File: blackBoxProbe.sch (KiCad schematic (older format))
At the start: 5 parts

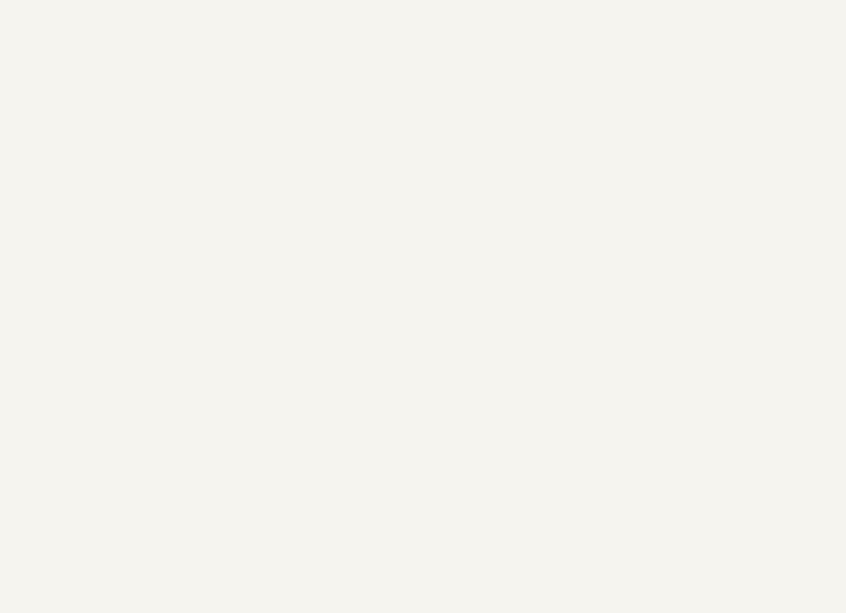
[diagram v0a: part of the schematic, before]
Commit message: * schematic layout of usb input and powersupply * PCB placing of usb input and powersupply
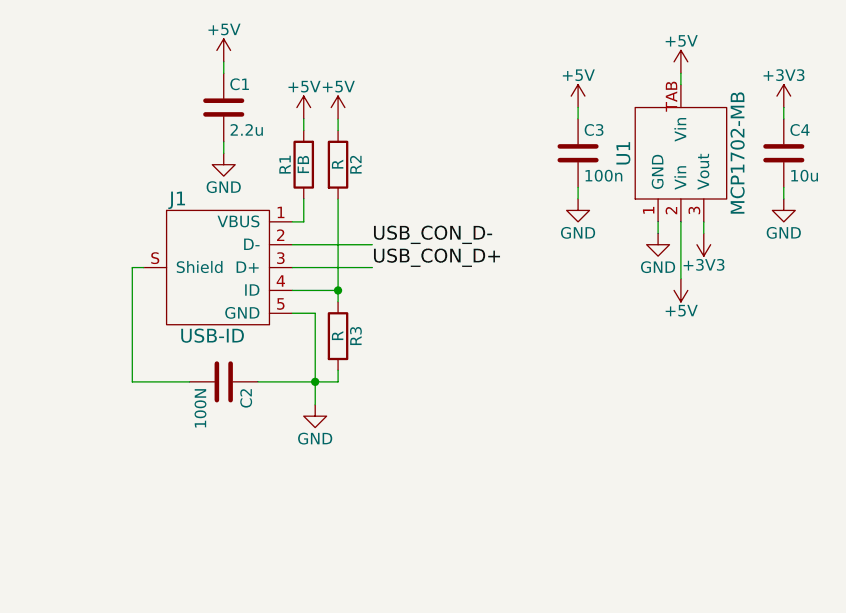
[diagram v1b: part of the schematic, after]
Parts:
- added C1: 2.2u, SquantorRcl:C_0805, symbol C
- added C2: 100N, SquantorRcl:C_0805, symbol C
- added C3: 100n, SquantorRcl:C_0603, symbol C
- added C4: 10u, SquantorRcl:C_0805, symbol C
- added J1: USB-ID, SquantorUsb:SquantorUsb-USB-UB-SMD4H, symbol USB-ID
- added R1: FB, SquantorRcl:R_0603_hand, symbol R
- added R2, R3: R, SquantorRcl:R_0603_hand, symbol R
- added U1: MCP1702-MB, SquantorMicrochip:MB-(SOT-89), symbol MCP1702-MB
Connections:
- new net: J1.1 (VBUS), R1.1
- new net: J1.4 (ID), R2.2, R3.1
- new net: C2.2, J1.S (Shield)
- new net +3V3: C4.1, U1.3 (Vout)
- new net +5V: C1.1, C3.1, R1.2, R2.1, U1.2 (Vin), U1.TAB (Vin)
- new net GND: C1.2, C2.1, C3.2, C4.2, J1.5 (GND), R3.2, U1.1 (GND)
- new net USB_CON_D+: J1.3 (D+)
- new net USB_CON_D-: J1.2 (D-)

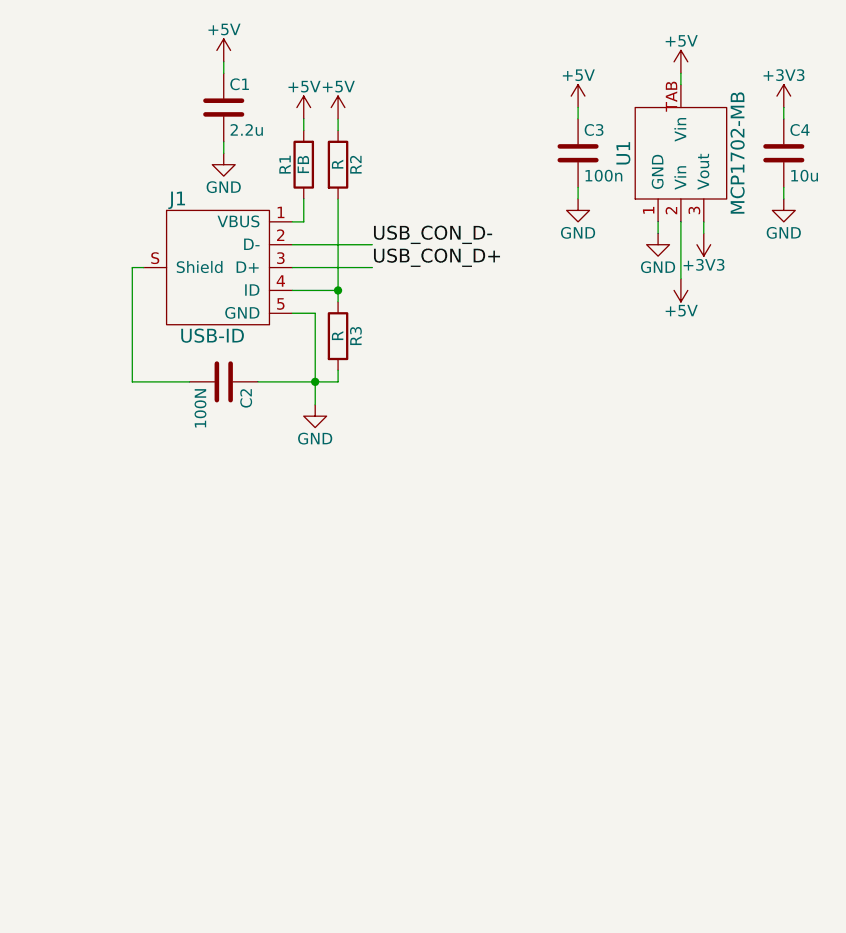
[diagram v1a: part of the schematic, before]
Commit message: * added usb protection diode
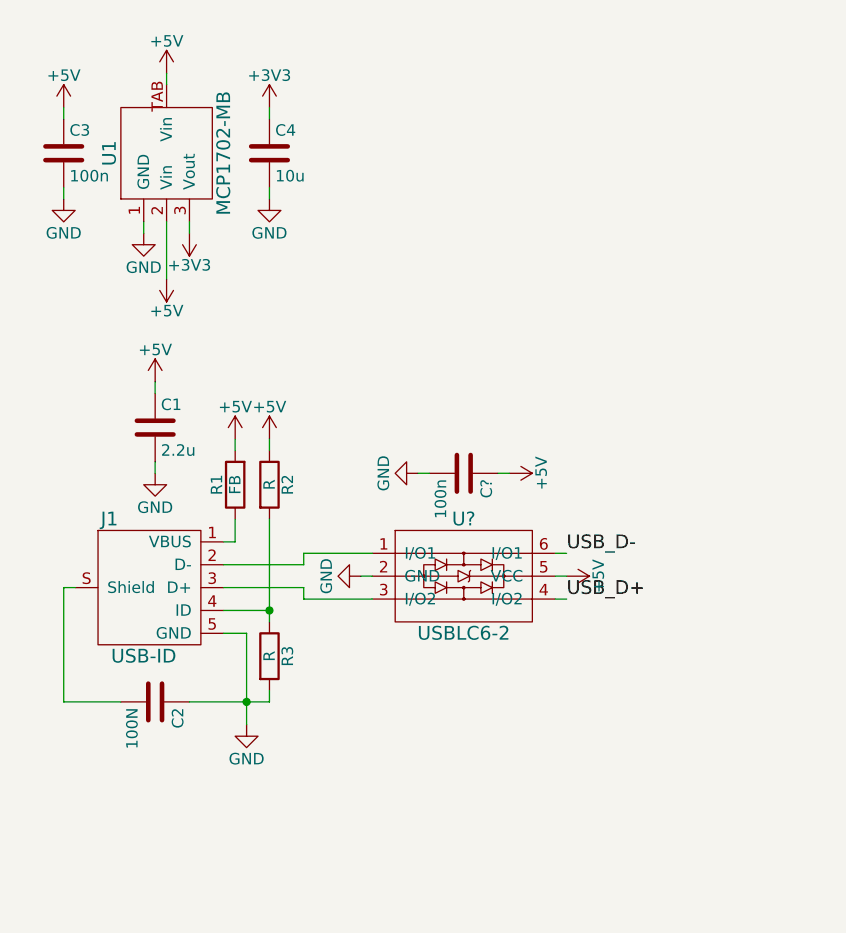
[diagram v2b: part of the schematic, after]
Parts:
- added C?: 100n, SquantorRcl:C_0603, symbol C
- added U?: USBLC6-2, symbol USBLC6-2
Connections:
- net +5V: now also C?.1, U?.5 (VCC)
- net GND: now also C?.2, U?.2 (GND)
- net USB_CON_D+: no longer names the net of J1.3 (D+)
- net USB_CON_D+: now also U?.3 (I/O2)
- net USB_CON_D-: no longer names the net of J1.2 (D-)
- net USB_CON_D-: now also U?.1 (I/O1)
- new net USB_D+: U?.4 (I/O2)
- new net USB_D-: U?.6 (I/O1)
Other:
- moved on the sheet: C1, C2, C3, C4, J1, R1, R2, R3, U1

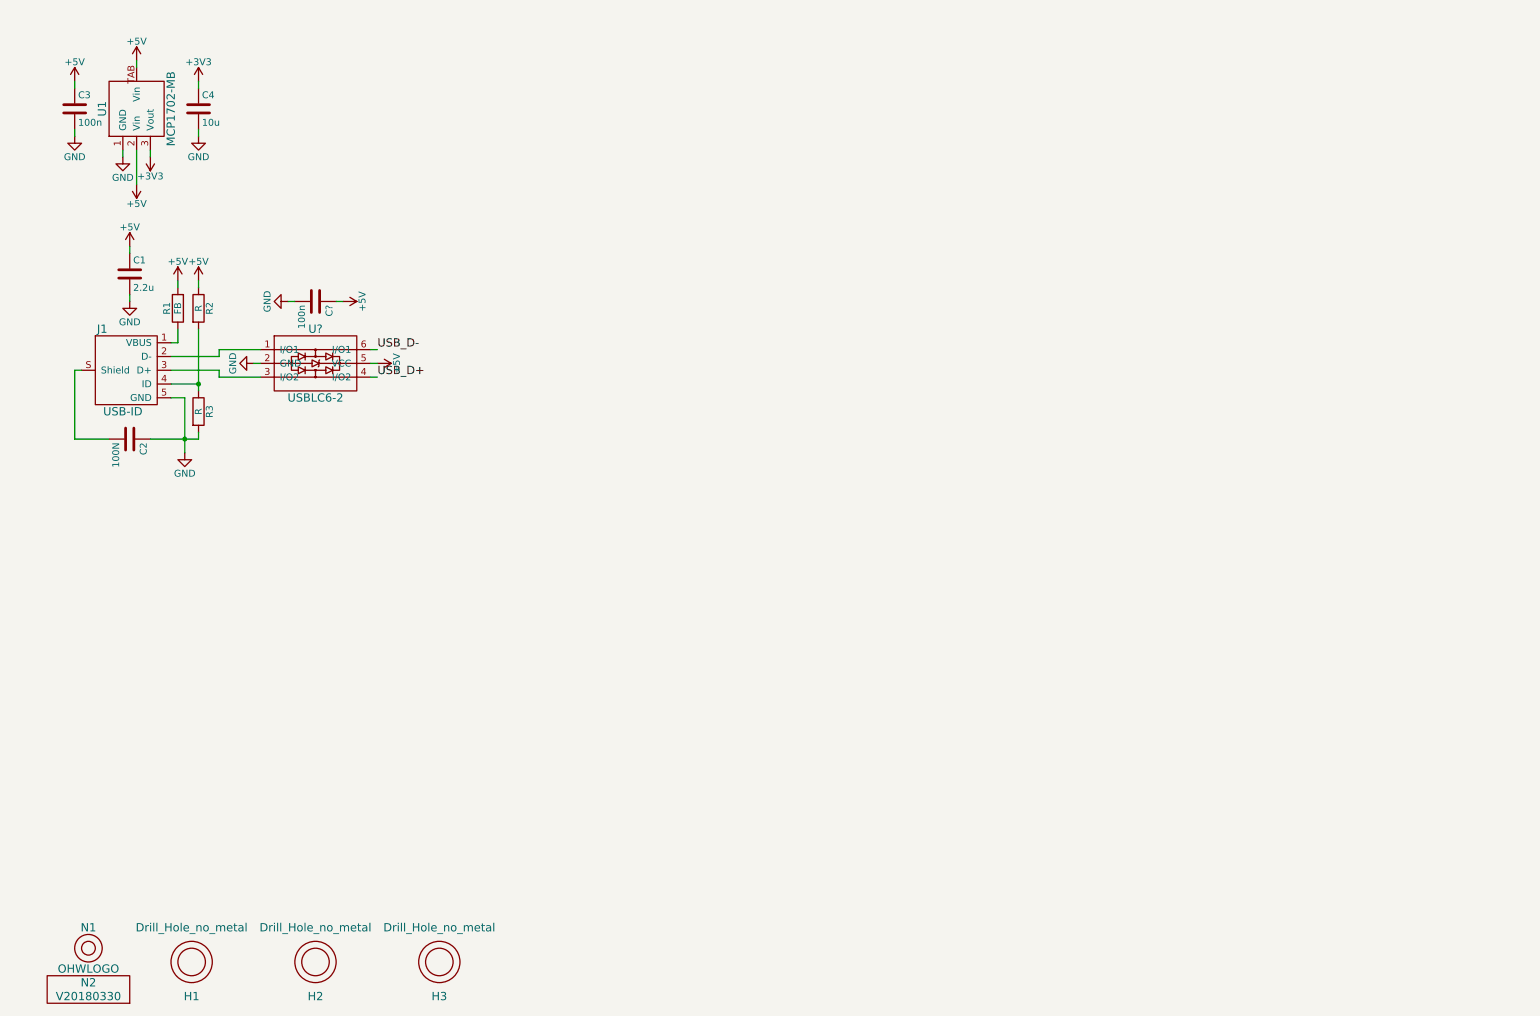
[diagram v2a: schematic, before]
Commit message: * placed controller and schematic entry of microcontroller power
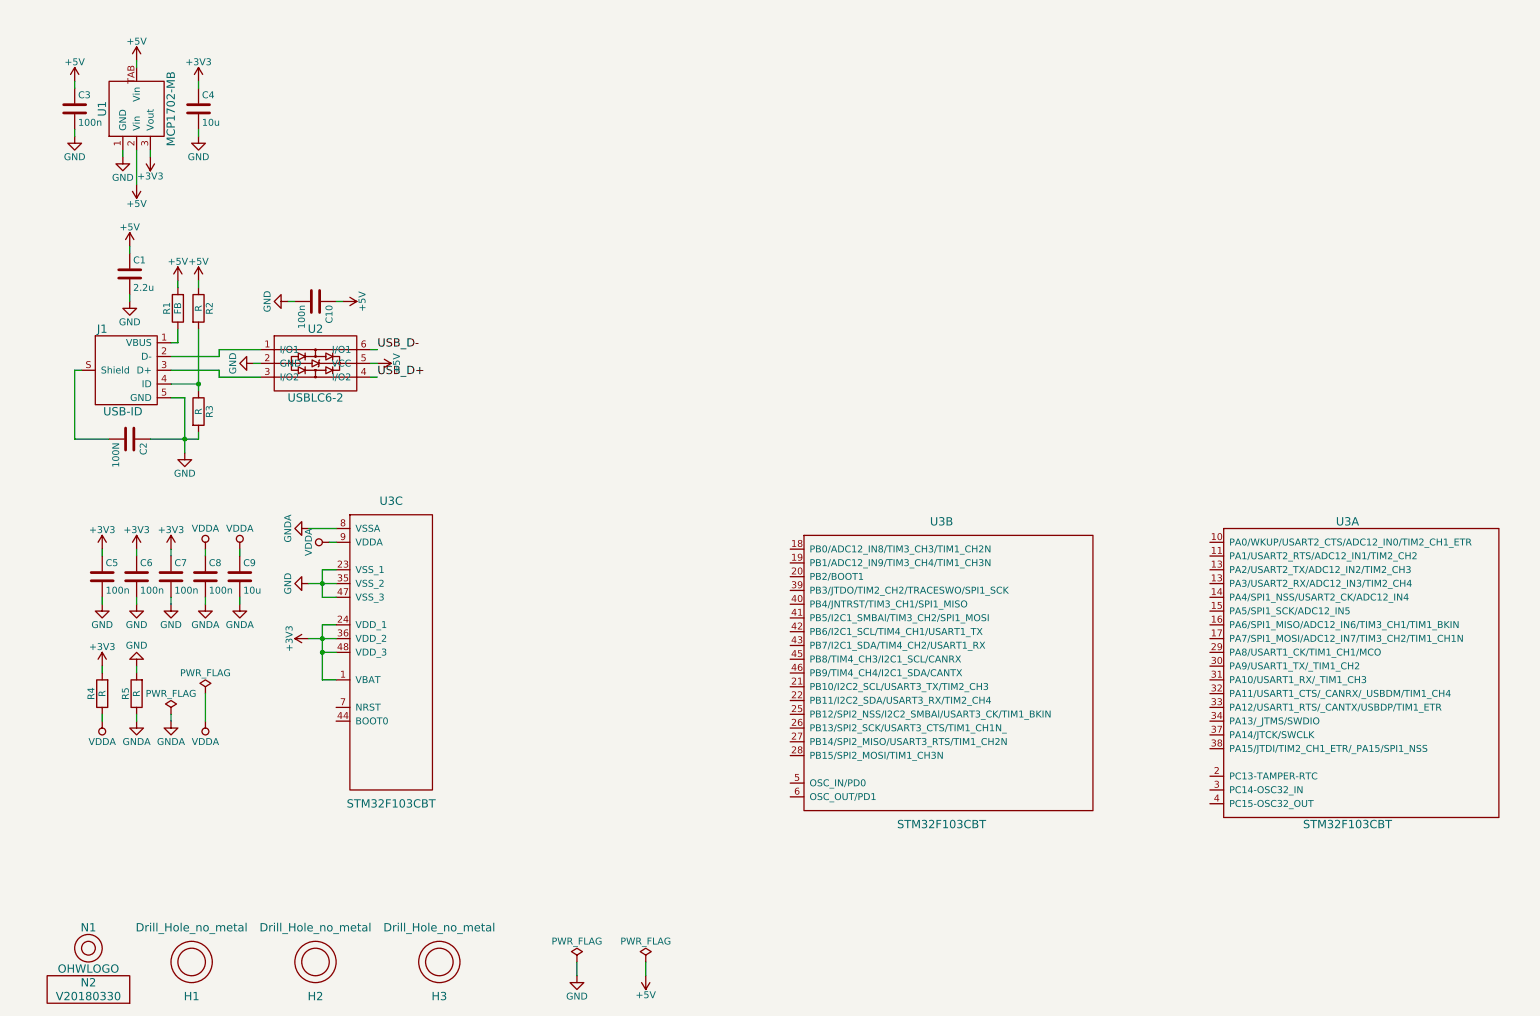
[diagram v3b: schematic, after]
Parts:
- added C5, C6, C7, C8: 100n, SquantorRcl:C_0603, symbol C
- added C9: 10u, SquantorRcl:C_0805, symbol C
- added R4, R5: R, SquantorRcl:R_0603_hand, symbol R
- added U3: STM32F103CBT, symbol STM32F103CBT
- gave numbers to parts that had none: 2
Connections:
- net +3V3: now also C5.1, C6.1, C7.1, R4.2, U3.1 (VBAT), U3.24 (VDD_1), U3.36 (VDD_2), U3.48 (VDD_3)
- net GND: now also C5.2, C6.2, C7.2, R5.2, U3.23 (VSS_1), U3.35 (VSS_2), U3.47 (VSS_3)
- new net GNDA: C8.2, C9.2, R5.1, U3.8 (VSSA)
- new net VDDA: C8.1, C9.1, R4.1, U3.9 (VDDA)

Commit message: WIP: further copying of the black box probe schematic
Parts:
- added C? (x2): C, symbol C
- added R? (x2): R, SquantorRcl:R_0603_hand, symbol R
- added R? (x2): 10K, SquantorRcl:R_0603_hand, symbol R
- added R?: 1.5K, SquantorRcl:R_0603_hand, symbol R
- added S? (x2): 2pin_tact_switch, SquantorButtons:SquantorButtons-DTSM3, symbol 2pin_tact_switch
- added Y?: Crystal, symbol Crystal
- U3: footprint (none) -> SquantorIC:SOT313-2
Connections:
- net +3V3: now also U3.40 (PB4/JNTRST/TIM3_CH1/SPI1_MISO), U3.41 (PB5/I2C1_SMBAl/TIM3_CH2/SPI1_MOSI), U3.42 (PB6/I2C1_SCL/TIM4_CH1/USART1_TX), R?.1
- net +5V: now also R?.1
- net GND: now also C?.2, C?.2, R?.1, R?.2, S?.1, S?.1
- net USB_D+: now also U3.33 (PA12/USART1_RTS/_CANTX/USBDP/TIM1_ETR), R?.2
- net USB_D-: now also U3.32 (PA11/USART1_CTS/_CANRX/_USBDM/TIM1_CH4)
- net PROBE_TMS_DIR: now reaches U3.11 (PA1/USART2_RTS/ADC12_IN1/TIM2_CH2)
- net PROBE_I_TDI: now reaches U3.13 (PA3/USART2_RX/ADC12_IN3/TIM2_CH4)
- net PROBE_I_TMS: now reaches U3.14 (PA4/SPI1_NSS/USART2_CK/ADC12_IN4)
- net PROBE_I_TCK: now reaches U3.15 (PA5/SPI1_SCK/ADC12_IN5)
- net PROBE_I_TDO: now reaches U3.16 (PA6/SPI1_MISO/ADC12_IN6/TIM3_CH1/TIM1_BKIN)
- net PROBE_I_RST_SEN: now reaches U3.17 (PA7/SPI1_MOSI/ADC12_IN7/TIM3_CH2/TIM1_CH1N)
- net USB_PU: now reaches U3.29 (PA8/USART1_CK/TIM1_CH1/MCO)
- net USB_PU: now also R?.1
- net PROBE_I_RX: now reaches U3.30 (PA9/USART1_TX/_TIM1_CH2)
- net PROBE_I_TX: now reaches U3.31 (PA10/USART1_RX/_TIM1_CH3)
- net MCU_SWDIO: now reaches U3.34 (PA13/_JTMS/SWDIO)
- net MCU_SWCLK: now reaches U3.37 (PA14/JTCK/SWCLK)
- net MCU_TDI: now reaches U3.38 (PA15/JTDI/TIM2_CH1_ETR/_PA15/SPI1_NSS)
- net LED0: now reaches U3.20 (PB2/BOOT1)
- net LED1: now reaches U3.21 (PB10/I2C2_SCL/USART3_TX/TIM2_CH3)
- net LED2: now reaches U3.22 (PB11/I2C2_SDA/USART3_RX/TIM2_CH4)
- net BUTTON: now reaches U3.25 (PB12/SPI2_NSS/I2C2_SMBAl/USART3_CK/TIM1_BKIN)
- net BUTTON: now also R?.2, S?.2
- net USB_V: now reaches U3.26 (PB13/SPI2_SCK/USART3_CTS/TIM1_CH1N_)
- net USB_V: now also R?.1, R?.2
- net MCU_TDO: now reaches U3.39 (PB3/JTDO/TIM2_CH2/TRACESWO/SPI1_SCK)
- net at U3.5 (OSC_IN/PD0): now also C?.1, Y?.1
- net at U3.6 (OSC_OUT/PD1): now also C?.1, Y?.2
- net at U3.44 (BOOT0): now also R?.2, S?.2
- net MCU_RST: now reaches U3.7 (NRST)
- new net PROBE_I_RST: U3.13 (PA3/USART2_RX/ADC12_IN3/TIM2_CH4)
